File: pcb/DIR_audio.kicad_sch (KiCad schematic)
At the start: 36 parts, among them J4 Conn_01x07_Pin, J5 Screw_Terminal_01x02, J6 Conn_Coaxial, U6 Si4735-D60-GU, U7 PAM8406D, Y1 opt.

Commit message: Add missing vendor
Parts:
- LS1, LS2: Vendor DigiKey -> HTL, DigiKey; VendorId 2056-K50FLS-8OHM-ND -> 103421, 2056-K50FLS-8OHM-ND
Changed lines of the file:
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@@
       (effects (font (size 1.27 1.27)) hide)
     )
-    (property "Vendor" "DigiKey" (at 48.26 92.71 0)
-      (effects (font (size 1.27 1.27)) hide)
-    )
-    (property "VendorId" "2056-K50FLS-8OHM-ND" (at 48.26 92.71 0)
+    (property "Vendor" "HTL, DigiKey" (at 48.26 92.71 0)
+      (effects (font (size 1.27 1.27)) hide)
+    )
+    (property "VendorId" "103421, 2056-K50FLS-8OHM-ND" (at 48.26 92.71 0)
       (effects (font (size 1.27 1.27)) hide)
     )
@@
       (effects (font (size 1.27 1.27)) hide)
     )
-    (property "Vendor" "DigiKey" (at 48.26 77.47 0)
-      (effects (font (size 1.27 1.27)) hide)
-    )
-    (property "VendorId" "2056-K50FLS-8OHM-ND" (at 48.26 77.47 0)
-      (effects (font (size 1.27 1.27)) hide)
-    )
+    (property "Vendor" "HTL, DigiKey" (at 48.26 77.47 0)
+      (effects (font (size 1.27 1.27)) hide)
+    )
+    (property "VendorId" "103421, 2056-K50FLS-8OHM-ND" (at 48.26 77.47 0)
+      (effects (font (size 1.27 1.27)) hide)
+    )

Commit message: Remove optional vendors
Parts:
- R33, R34, R36, R37: Vendor HTL -> (none); VendorId 102967 -> (none)
- Y1: Vendor HTL -> (none); VendorId 103447 -> (none)
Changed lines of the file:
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@@
       (effects (font (size 1.27 1.27)) hide)
     )
-    (property "Vendor" "HTL" (at 107.95 86.36 0)
-      (effects (font (size 1.27 1.27)) hide)
-    )
-    (property "VendorId" "102967" (at 107.95 86.36 0)
+    (property "Vendor" "" (at 107.95 86.36 0)
+      (effects (font (size 1.27 1.27)) hide)
+    )
+    (property "VendorId" "" (at 107.95 86.36 0)
       (effects (font (size 1.27 1.27)) hide)
     )
@@
       (effects (font (size 1.27 1.27)) hide)
     )
-    (property "Vendor" "HTL" (at 205.74 83.82 0)
-      (effects (font (size 1.27 1.27)) hide)
-    )
-    (property "VendorId" "103447" (at 205.74 83.82 0)
+    (property "Vendor" "" (at 205.74 83.82 0)
+      (effects (font (size 1.27 1.27)) hide)
+    )
+    (property "VendorId" "" (at 205.74 83.82 0)
       (effects (font (size 1.27 1.27)) hide)
     )
@@
       (effects (font (size 1.27 1.27)) hide)
     )
-    (property "Vendor" "HTL" (at 205.74 99.06 0)
-      (effects (font (size 1.27 1.27)) hide)
-    )
-    (property "VendorId" "102967" (at 205.74 99.06 0)
+    (property "Vendor" "" (at 205.74 99.06 0)
+      (effects (font (size 1.27 1.27)) hide)
+    )
+    (property "VendorId" "" (at 205.74 99.06 0)
       (effects (font (size 1.27 1.27)) hide)
     )
@@
       (effects (font (size 1.27 1.27)) hide)
     )
-    (property "Vendor" "HTL" (at 113.03 86.36 0)
-      (effects (font (size 1.27 1.27)) hide)
-    )
-    (property "VendorId" "102967" (at 113.03 86.36 0)
+    (property "Vendor" "" (at 113.03 86.36 0)
+      (effects (font (size 1.27 1.27)) hide)
+    )
+    (property "VendorId" "" (at 113.03 86.36 0)
       (effects (font (size 1.27 1.27)) hide)
     )
@@
       (effects (font (size 1.27 1.27)) hide)
     )
-    (property "Vendor" "HTL" (at 185.42 101.6 0)
-      (effects (font (size 1.27 1.27)) hide)
-    )
-    (property "VendorId" "102967" (at 185.42 101.6 0)
-      (effects (font (size 1.27 1.27)) hide)
-    )
+    (property "Vendor" "" (at 185.42 101.6 0)
+      (effects (font (size 1.27 1.27)) hide)
+    )
+    (property "VendorId" "" (at 185.42 101.6 0)
+      (effects (font (size 1.27 1.27)) hide)
+    )

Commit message: Fix wrong vendor-id
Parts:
- C30: VendorId 100128 -> 103328
- C31: VendorId 100128 -> 103325
- J4: VendorId 101521 -> 101545
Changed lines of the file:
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@@
       (effects (font (size 1.27 1.27)) hide)
     )
-    (property "VendorId" "100128" (at 149.86 109.22 0)
+    (property "VendorId" "103325" (at 149.86 109.22 0)
       (effects (font (size 1.27 1.27)) hide)
     )
@@
       (effects (font (size 1.27 1.27)) hide)
     )
-    (property "VendorId" "101521" (at 120.65 177.8 0)
+    (property "VendorId" "101545" (at 120.65 177.8 0)
       (effects (font (size 1.27 1.27)) hide)
     )
@@
       (effects (font (size 1.27 1.27)) hide)
     )
-    (property "VendorId" "100128" (at 144.78 102.87 0)
-      (effects (font (size 1.27 1.27)) hide)
-    )
+    (property "VendorId" "103328" (at 144.78 102.87 0)
+      (effects (font (size 1.27 1.27)) hide)
+    )

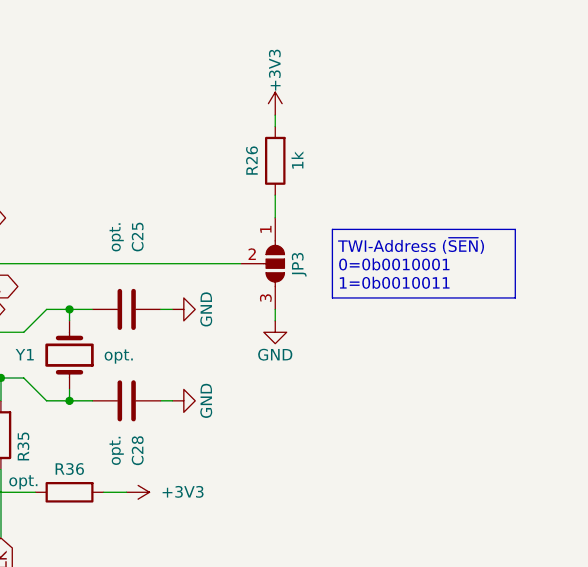
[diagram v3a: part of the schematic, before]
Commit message: Fix TWI address description
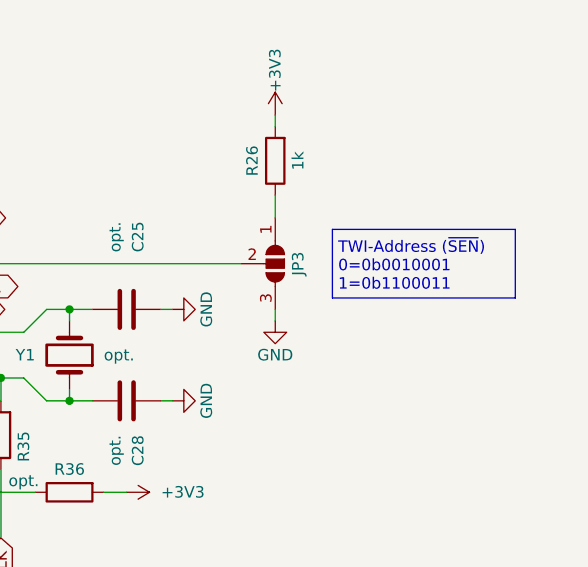
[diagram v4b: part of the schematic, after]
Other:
- note added: "TWI-Address (~{SEN}) 0=0b0010001 1=0b1100011"
- note removed: "TWI-Address (~{SEN}) 0=0b0010001 1=0b0010011"
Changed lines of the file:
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@@
     (effects (font (size 1.27 1.27)) (justify right bottom))
   )
-  (text "TWI-Address (~{SEN})\n0=0b0010001\n1=0b0010011" (at 235.585 76.835 0)
+  (text "TWI-Address (~{SEN})\n0=0b0010001\n1=0b1100011" (at 235.585 76.835 0)
     (effects (font (size 1.27 1.27)) (justify left bottom))
   )

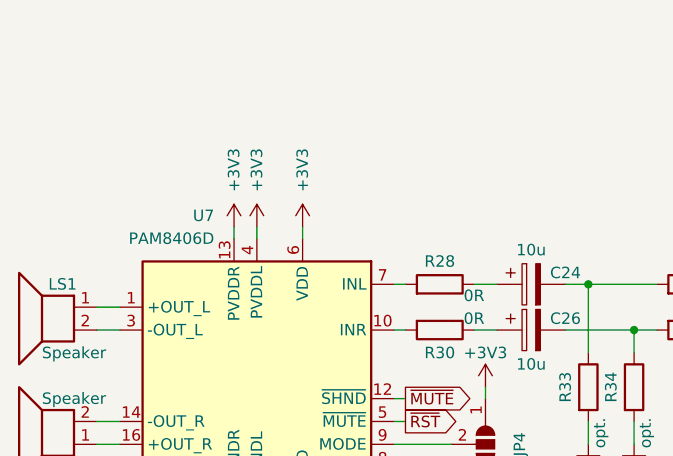
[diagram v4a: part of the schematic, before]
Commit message: Fix power path issue
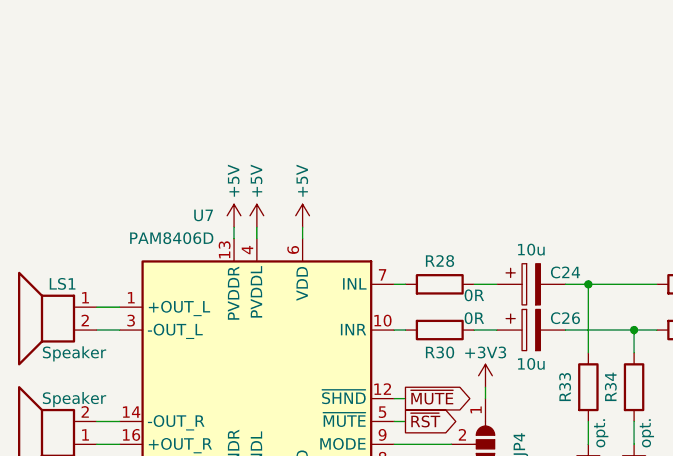
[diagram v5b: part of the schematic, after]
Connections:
- net +3V3: no longer U7.13 (PVDDR), U7.4 (PVDDL), U7.6 (VDD)
- new net +5V: U7.13 (PVDDR), U7.4 (PVDDL), U7.6 (VDD)
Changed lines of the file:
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@@
+    )
+  )
+  (symbol (lib_id "power:+5V") (at 76.2 68.58 0) (unit 1)
+    (in_bom yes) (on_board yes) (dnp no)
+    (property "Reference" "#PWR053" (at 76.2 72.39 0)
+      (effects (font (size 1.27 1.27)) hide)
+    )
+    (property "Value" "+5V" (at 76.2 63.5 90)
+      (effects (font (size 1.27 1.27)))
+    )
+    (property "Footprint" "" (at 76.2 68.58 0)
+      (effects (font (size 1.27 1.27)) hide)
+    )
+    (property "Datasheet" "" (at 76.2 68.58 0)
+      (effects (font (size 1.27 1.27)) hide)
+    )
+    (pin "1")
+    (instances
+      (project "DIR"
+        (path "/e63e39d7-6ac0-4ffd-8aa3-1841a4541b55/c39b484a-1cf1-42ca-b716-51ee80c35595"
+          (reference "#PWR053") (unit 1)
+        )
+      )
     )
   )
@@
         (path "/e63e39d7-6ac0-4ffd-8aa3-1841a4541b55/c39b484a-1cf1-42ca-b716-51ee80c35595"
           (reference "#PWR069") (unit 1)
-        )
-      )
-    )
-  )
-  (symbol (lib_id "power:+3V3") (at 71.12 68.58 0) (unit 1)
-    (in_bom yes) (on_board yes) (dnp no)
-    (property "Reference" "#PWR052" (at 71.12 72.39 0)
-      (effects (font (size 1.27 1.27)) hide)
-    )
-    (property "Value" "+3V3" (at 71.12 62.23 90)
-      (effects (font (size 1.27 1.27)))
-    )
-    (property "Footprint" "" (at 71.12 68.58 0)
-      (effects (font (size 1.27 1.27)) hide)
-    )
-    (property "Datasheet" "" (at 71.12 68.58 0)
-      (effects (font (size 1.27 1.27)) hide)
-    )
-    (pin "1")
-    (instances
-      (project "DIR"
-        (path "/e63e39d7-6ac0-4ffd-8aa3-1841a4541b55/c39b484a-1cf1-42ca-b716-51ee80c35595"
-          (reference "#PWR052") (unit 1)
         )
       )
@@
         (path "/e63e39d7-6ac0-4ffd-8aa3-1841a4541b55/c39b484a-1cf1-42ca-b716-51ee80c35595"
           (reference "R26") (unit 1)
+        )
+      )
+    )
+  )
+  (symbol (lib_id "power:+5V") (at 68.58 68.58 0) (unit 1)
+    (in_bom yes) (on_board yes) (dnp no)
+    (property "Reference" "#PWR052" (at 68.58 72.39 0)
+      (effects (font (size 1.27 1.27)) hide)
+    )
+    (property "Value" "+5V" (at 68.58 63.5 90)
+      (effects (font (size 1.27 1.27)))
+    )
+    (property "Footprint" "" (at 68.58 68.58 0)
+      (effects (font (size 1.27 1.27)) hide)
+    )
+    (property "Datasheet" "" (at 68.58 68.58 0)
+      (effects (font (size 1.27 1.27)) hide)
+    )
+    (pin "1")
+    (instances
+      (project "DIR"
+        (path "/e63e39d7-6ac0-4ffd-8aa3-1841a4541b55/c39b484a-1cf1-42ca-b716-51ee80c35595"
+          (reference "#PWR052") (unit 1)
         )
       )
@@
         (path "/e63e39d7-6ac0-4ffd-8aa3-1841a4541b55/c39b484a-1cf1-42ca-b716-51ee80c35595"
           (reference "R27") (unit 1)
-        )
-      )
-    )
-  )
-  (symbol (lib_id "power:+3V3") (at 76.2 68.58 0) (unit 1)
-    (in_bom yes) (on_board yes) (dnp no)
-    (property "Reference" "#PWR053" (at 76.2 72.39 0)
-      (effects (font (size 1.27 1.27)) hide)
-    )
-    (property "Value" "+3V3" (at 76.2 62.23 90)
-      (effects (font (size 1.27 1.27)))
-    )
-    (property "Footprint" "" (at 76.2 68.58 0)
-      (effects (font (size 1.27 1.27)) hide)
-    )
-    (property "Datasheet" "" (at 76.2 68.58 0)
-      (effects (font (size 1.27 1.27)) hide)
-    )
-    (pin "1")
-    (instances
-      (project "DIR"
-        (path "/e63e39d7-6ac0-4ffd-8aa3-1841a4541b55/c39b484a-1cf1-42ca-b716-51ee80c35595"
-          (reference "#PWR053") (unit 1)
         )
       )
@@
         (path "/e63e39d7-6ac0-4ffd-8aa3-1841a4541b55/c39b484a-1cf1-42ca-b716-51ee80c35595"
           (reference "R28") (unit 1)
-        )
-      )
-    )
-  )
-  (symbol (lib_id "power:+3V3") (at 68.58 68.58 0) (unit 1)
-    (in_bom yes) (on_board yes) (dnp no)
-    (property "Reference" "#PWR051" (at 68.58 72.39 0)
-      (effects (font (size 1.27 1.27)) hide)
-    )
-    (property "Value" "+3V3" (at 68.58 62.23 90)
-      (effects (font (size 1.27 1.27)))
-    )
-    (property "Footprint" "" (at 68.58 68.58 0)
-      (effects (font (size 1.27 1.27)) hide)
-    )
-    (property "Datasheet" "" (at 68.58 68.58 0)
-      (effects (font (size 1.27 1.27)) hide)
-    )
-    (pin "1")
-    (instances
-      (project "DIR"
-        (path "/e63e39d7-6ac0-4ffd-8aa3-1841a4541b55/c39b484a-1cf1-42ca-b716-51ee80c35595"
-          (reference "#PWR051") (unit 1)
         )
       )
@@
         )
       )
+    )
+  )
+  (symbol (lib_id "power:+5V") (at 71.12 68.58 0) (unit 1)
+    (in_bom yes) (on_board yes) (dnp no)
+    (property "Reference" "#PWR051" (at 71.12 72.39 0)
+      (effects (font (size 1.27 1.27)) hide)
+    )
+    (property "Value" "+5V" (at 71.12 63.5 90)
+      (effects (font (size 1.27 1.27)))
+    )
+    (property "Footprint" "" (at 71.12 68.58 0)
+      (effects (font (size 1.27 1.27)) hide)
+    )
+    (property "Datasheet" "" (at 71.12 68.58 0)
+      (effects (font (size 1.27 1.27)) hide)
+    )
+    (pin "1")
+    (instances
+      (project "DIR"
+        (path "/e63e39d7-6ac0-4ffd-8aa3-1841a4541b55/c39b484a-1cf1-42ca-b716-51ee80c35595"
+          (reference "#PWR051") (unit 1)
+        )
+      )

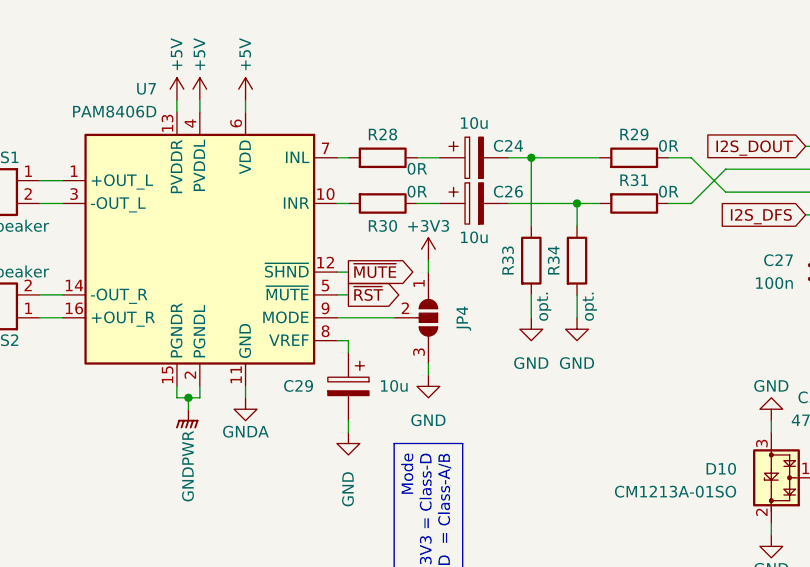
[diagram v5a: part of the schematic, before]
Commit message: Change SHDN and MUTE pins
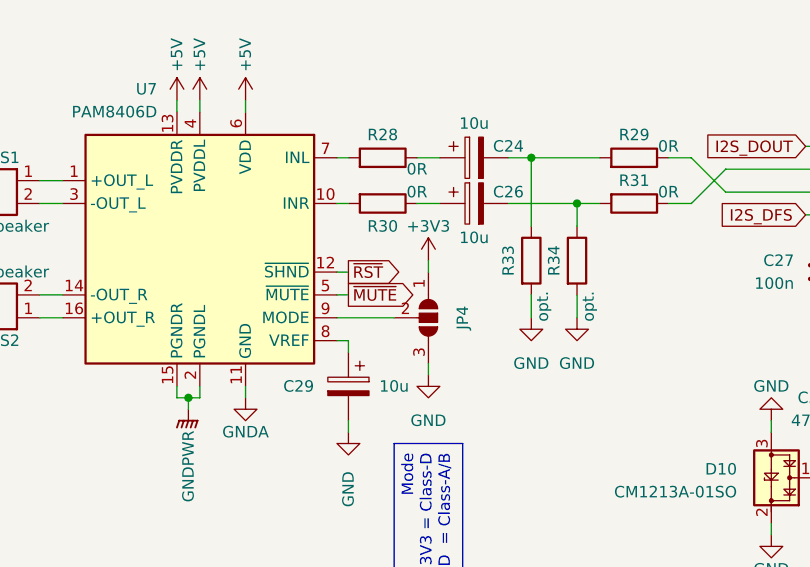
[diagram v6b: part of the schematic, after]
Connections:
- net ~{MUTE}: now also U7.5 (~{MUTE}); no longer U7.12 (~{SHND})
- net ~{RST}: now also U7.12 (~{SHND}); no longer U7.5 (~{MUTE})
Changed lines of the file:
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@@
     )
   )
-  (global_label "~{MUTE}" (shape output) (at 87.63 87.63 0) (fields_autoplaced)
+  (global_label "~{MUTE}" (shape output) (at 87.63 90.17 0) (fields_autoplaced)
     (effects (font (size 1.27 1.27)) (justify left))
-    (property "Intersheetrefs" "${INTERSHEET_REFS}" (at 95.5137 87.63 0)
+    (property "Intersheetrefs" "${INTERSHEET_REFS}" (at 95.5137 90.17 0)
       (effects (font (size 1.27 1.27)) (justify left) hide)
     )
@@
     )
   )
-  (global_label "~{RST}" (shape output) (at 87.63 90.17 0) (fields_autoplaced)
+  (global_label "~{RST}" (shape output) (at 87.63 87.63 0) (fields_autoplaced)
     (effects (font (size 1.27 1.27)) (justify left))
-    (property "Intersheetrefs" "${INTERSHEET_REFS}" (at 94.0623 90.17 0)
+    (property "Intersheetrefs" "${INTERSHEET_REFS}" (at 94.0623 87.63 0)
       (effects (font (size 1.27 1.27)) (justify left) hide)
     )
